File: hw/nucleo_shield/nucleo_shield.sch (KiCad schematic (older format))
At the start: 20 parts, among them CN101 Nucleo-F411RE-CN10, CN71 Nucleo-F411RE-CN7, P12 CONN_RS485_OUT, P13 CONN_RS485_IN, P15 CONN_ANALOG, P16 CONN_EXTI2C, P17 CONN_EXT, P18 CONN_1WIRE, P4 POWER_CON, P6 ETH_CONN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

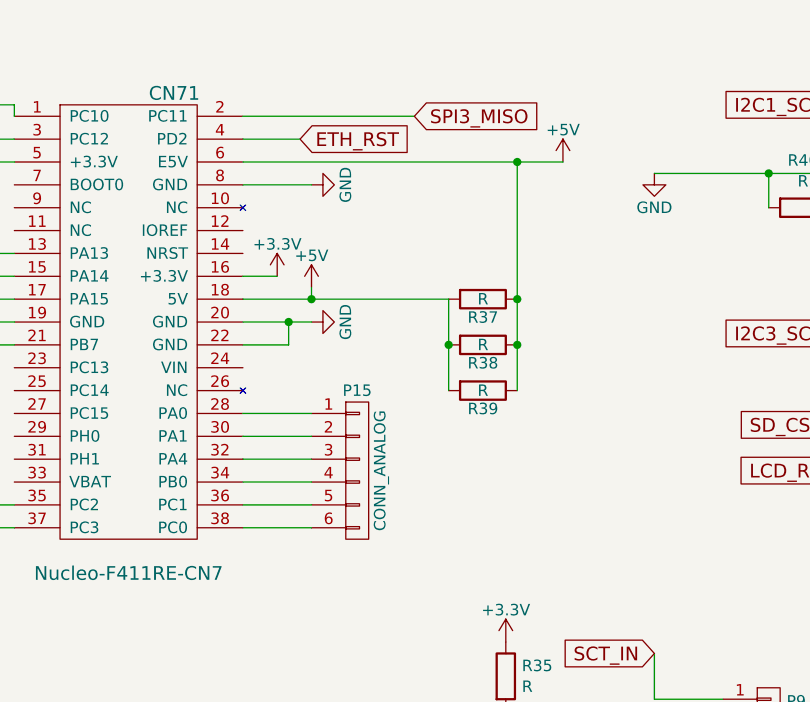
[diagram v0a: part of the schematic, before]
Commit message: Nucleo shield: mino modifications
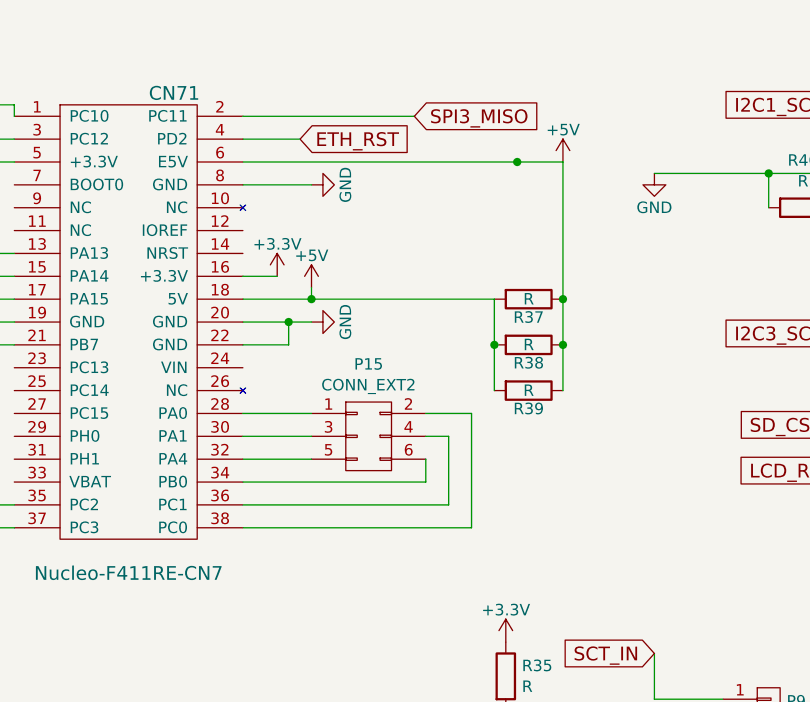
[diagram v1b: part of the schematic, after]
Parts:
- removed P15: CONN_ANALOG, Pin_Headers:Pin_Header_Straight_1x06, symbol CONN_01X06
- added P15: CONN_EXT2, Pin_Headers:Pin_Header_Straight_2x03, symbol CONN_02X03
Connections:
- net at CN71.28 (PA0): now also P15.1 (P1)
- net at CN71.30 (PA1): now also P15.3 (P3)
- net at CN71.32 (PA4): now also P15.5 (P5)
- net at CN71.34 (PB0): now also P15.6 (P6)
- net at CN71.36 (PC1): now also P15.4 (P4)
- net at CN71.38 (PC0): now also P15.2 (P2)
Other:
- moved on the sheet: R37, R38, R39

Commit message: Nucleo: add more extension header for SPI, etc
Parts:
- added P19: CONN_EXT_SPI, Pin_Headers:Pin_Header_Straight_1x06, symbol CONN_01X06
- added R41: R, Resistors_ThroughHole:Resistor_Horizontal_RM10mm, symbol R
- P16: footprint Pin_Headers:Pin_Header_Straight_1x04 -> Pin_Headers:Pin_Header_Straight_1x05; symbol CONN_01X04 -> CONN_01X05
- R39: footprint Resistors_ThroughHole:Resistor_Horizontal_RM20mm -> Resistors_ThroughHole:Resistor_Horizontal_RM15mm
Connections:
- net +5V: now also P19.2 (P2)
- net GND: now also P19.1 (P1), R41.1, R41.2
- net I2C1_SCL: now also P16.4 (P4); no longer P16.3 (P3)
- net I2C1_SDA: now also P16.5 (P5); no longer P16.4 (P4)
- net RS_DE: now also CN71.25 (PC14); no longer CN71.15 (PA14)
- net RS_RX: now also CN71.21 (PB7); no longer CN71.17 (PA15)
- net RS_TX: now also CN71.17 (PA15); no longer CN71.21 (PB7)
- net SPI3_MISO: now also P19.4 (P4)
- net SPI3_MOSI: now also P19.6 (P6)
- net SPI3_SCK: now also P19.5 (P5)
- net I2C_GPIO: now reaches CN101.1 (PC9)
- net I2C_GPIO: now also P16.3 (P3)
- new net EXT_SPI_SS: CN71.15 (PA14), P19.3 (P3)
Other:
- moved on the sheet: P13, P4

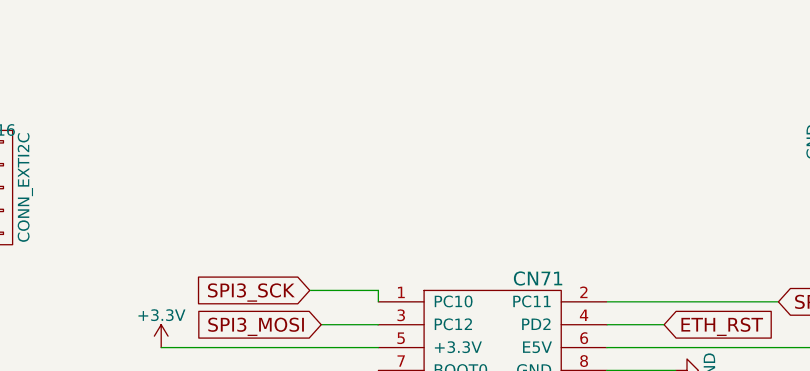
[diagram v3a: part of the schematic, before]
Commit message: Nucleo: add BME180 header on PCB
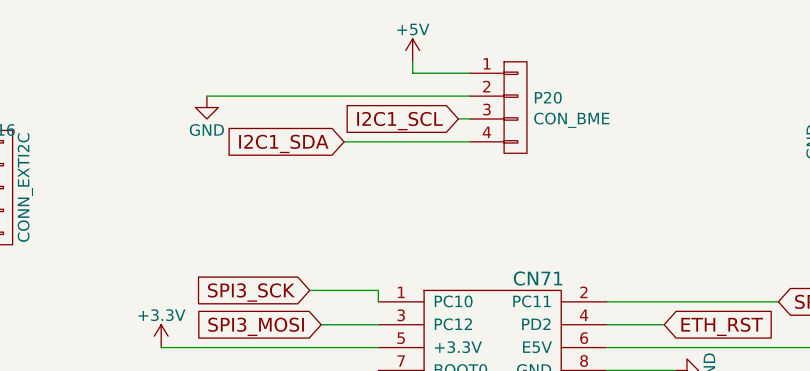
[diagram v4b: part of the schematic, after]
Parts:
- added P20: CON_BME, Pin_Headers:Pin_Header_Straight_1x04, symbol CONN_01X04
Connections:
- net +5V: now also P20.1 (P1)
- net GND: now also P20.2 (P2)
- net I2C1_SCL: now also P20.3 (P3)
- net I2C1_SDA: now also P20.4 (P4)
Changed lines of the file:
@@
 Connection ~ 8000 2200
 Connection ~ 8300 2200
+$Comp
+L CONN_01X04 P20
+U 1 1 57419091
+P 5300 950
+F 0 "P20" H 5378 991 50  0000 L CNN
+F 1 "CON_BME" H 5378 900 50  0000 L CNN
+F 2 "Pin_Headers:Pin_Header_Straight_1x04" H 5300 950 50  0001 C CNN
+F 3 "" H 5300 950 50  0000 C CNN
+	1    5300 950
+	1    0    0    -1
+$EndComp
+Text GLabel 5050 1000 0    60   Input ~ 0
+I2C1_SCL
+Text GLabel 4550 1100 0    60   Input ~ 0
+I2C1_SDA
+Wire Wire Line
+	4550 1100 5100 1100
+Wire Wire Line
+	5100 1000 5050 1000
+$Comp
+L GND #PWR027
+U 1 1 5741922D
+P 3950 900
+F 0 "#PWR027" H 3950 650 50  0001 C CNN
+F 1 "GND" H 3950 750 50  0000 C CNN
+F 2 "" H 3950 900 60  0000 C CNN
+F 3 "" H 3950 900 60  0000 C CNN
+	1    3950 900
+	1    0    0    -1
+$EndComp
+Wire Wire Line
+	5100 900  3950 900
+$Comp
+L +5V #PWR028
+U 1 1 57419326
+P 4850 750
+F 0 "#PWR028" H 4850 600 50  0001 C CNN
+F 1 "+5V" H 4850 890 50  0000 C CNN
+F 2 "" H 4850 750 60  0000 C CNN
+F 3 "" H 4850 750 60  0000 C CNN
+	1    4850 750
+	1    0    0    -1
+$EndComp
+Wire Wire Line
+	4850 750  4850 800
+Wire Wire Line
+	4850 800  5100 800
 $EndSCHEMATC

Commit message: Nucleo: ad vias
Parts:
- removed R37, R38, R40, R41: R, Resistors_ThroughHole:Resistor_Horizontal_RM10mm, symbol R
- removed R39: R, Resistors_ThroughHole:Resistor_Horizontal_RM15mm, symbol R
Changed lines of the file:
@@
 SD_CS
-$Comp
-L R R37
-U 1 1 573365D0
-P 6950 2600
-F 0 "R37" V 7030 2600 50  0000 C CNN
-F 1 "R" V 6950 2600 50  0000 C CNN
-F 2 "Resistors_ThroughHole:Resistor_Horizontal_RM10mm" V 6880 2600 30  0001 C CNN
-F 3 "" H 6950 2600 30  0000 C CNN
-	1    6950 2600
-	0    1    1    0
-$EndComp
-$Comp
-L R R38
-U 1 1 57336EF7
-P 6950 2800
-F 0 "R38" V 7030 2800 50  0000 C CNN
-F 1 "R" V 6950 2800 50  0000 C CNN
-F 2 "Resistors_ThroughHole:Resistor_Horizontal_RM10mm" V 6880 2800 30  0001 C CNN
-F 3 "" H 6950 2800 30  0000 C CNN
-	1    6950 2800
-	0    1    1    0
-$EndComp
 $Comp
 L CONN_01X05 P17
@@
 Text GLabel 8300 1750 0    60   Input ~ 0
 I2C1_SCL
-$Comp
-L R R40
-U 1 1 5733E4B6
-P 8150 2200
-F 0 "R40" V 7943 2200 50  0000 C CNN
-F 1 "R" V 8034 2200 50  0000 C CNN
-F 2 "Resistors_ThroughHole:Resistor_Horizontal_RM10mm" V 8080 2200 50  0001 C CNN
-F 3 "" H 8150 2200 50  0000 C CNN
-	1    8150 2200
-	0    1    1    0
-$EndComp
 Text GLabel 3950 3500 0    60   Input ~ 0
 1WIRE_IN
@@
 	1    4300 4750
 	1    0    0    -1
-$EndComp
-$Comp
-L R R39
-U 1 1 5733CEEB
-P 6950 3000
-F 0 "R39" V 7030 3000 50  0000 C CNN
-F 1 "R" V 6950 3000 50  0000 C CNN
-F 2 "Resistors_ThroughHole:Resistor_Horizontal_RM15mm" V 6880 3000 30  0001 C CNN
-F 3 "" H 6950 3000 30  0000 C CNN
-	1    6950 3000
-	0    1    1    0
 $EndComp
 $Comp
@@
 	4500 2700 4700 2700
 Wire Wire Line
-	5700 2600 6800 2600
+	5700 2600 6900 2600
 Wire Wire Line
 	6000 2600 6000 2550
@@
 	8850 1850 8950 1850
 Wire Wire Line
-	8000 2050 8000 2450
-Connection ~ 8000 2050
-Wire Wire Line
-	8300 2050 8300 2450
-Connection ~ 8300 2050
-Wire Wire Line
-	7100 2000 7100 3000
-Wire Wire Line
-	6800 2600 6800 3000
-Connection ~ 7100 2600
-Wire Wire Line
 	3950 3500 4700 3500
 Wire Wire Line
@@
 Wire Wire Line
 	4300 4650 4300 4750
-Connection ~ 6800 2800
-Connection ~ 7100 2800
 Wire Wire Line
 	6600 3500 6600 3200
@@
 Wire Wire Line
 	4650 6550 4650 6600
-$Comp
-L R R41
-U 1 1 5734C48B
-P 8150 2450
-F 0 "R41" V 7943 2450 50  0000 C CNN
-F 1 "R" V 8034 2450 50  0000 C CNN
-F 2 "Resistors_ThroughHole:Resistor_Horizontal_RM10mm" V 8080 2450 50  0001 C CNN
-F 3 "" H 8150 2450 50  0000 C CNN
-	1    8150 2450
-	0    1    1    0
-$EndComp
-Connection ~ 8000 2200
-Connection ~ 8300 2200
 $Comp
 L CONN_01X04 P20
@@
 Wire Wire Line
 	4850 800  5100 800
+Wire Wire Line
+	6900 2600 6900 2000
 $EndSCHEMATC

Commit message: WIP: add more IO
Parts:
- removed P17: CONN_EXT, Pin_Headers:Pin_Header_Straight_1x05, symbol CONN_01X05
- added P3: POWER_24V_CON, w_conn_screw:mors_2p, symbol CONN_01X02
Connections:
- net SRLatch2: now reaches CN101.12 (PA12)
- net SRDATA2: now reaches CN101.14 (PA11)
- net I2C1_GPIO: now reaches CN101.2 (PC8)
- net SRCLK2: now reaches CN101.6 (PC5)
- new net +24V: P3.2 (P2)
- new net GND_24V: P3.1 (P1)

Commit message: HW: rework of nucleo shield to add more IOs
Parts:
- added P14: CONN_02X06, Pin_Headers:Pin_Header_Straight_2x06, symbol CONN_02X06
- R35, R36: footprint Resistors_ThroughHole:Resistor_Horizontal_RM10mm -> Resistors_SMD:R_0805_HandSoldering
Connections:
- net +3V3: no longer CN71.5 (+3.3V)
- net GND: now also P14.10 (P10), P14.12 (P12), P14.2 (P2), P14.4 (P4), P14.6 (P6), P14.8 (P8); no longer P6.8 (P8)
- net I2C1_GPIO: now also CN101.1 (PC9); no longer CN101.2 (PC8)
- net I2C1_SCL: now also P20.4 (P4); no longer P20.3 (P3)
- net I2C1_SDA: now also P16.3 (P3), P20.3 (P3); no longer P16.5 (P5), P20.4 (P4)
- net I2C_GPIO: now also CN101.2 (PC8), P16.5 (P5); no longer CN101.1 (PC9), P16.3 (P3)
- net SRCLK: now also CN101.17 (PB6); no longer CN101.16 (PB12)
- net PA5: now reaches CN101.11 (PA5)
- net PA5: now also P14.3 (P3)
- net PA6: now reaches CN101.13 (PA6)
- net PA6: now also P14.7 (P7)
- net PA7: now reaches CN101.15 (PA7)
- net PA7: now also P14.11 (P11)
- net SRCLK2: no longer names the net of CN101.6 (PC5)
- net SRDATA2 renamed PA11
- net PA11: now also P14.5 (P5)
- net SRLatch2 renamed PA12
- net PA12: now also P14.1 (P1)
- new net PB12: CN101.16 (PB12), P14.9 (P9)
